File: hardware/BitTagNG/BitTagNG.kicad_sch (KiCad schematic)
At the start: 22 parts, among them J201 CONN_02X04, J301 Conn_01x01, J302 Conn_01x01, J303 Conn_01x01, J304 Conn_01x01, J401 CONN_01X02, Q501 Q_NPN_BEC, U1 at25ex321D-UUN, U2 adxl367, U302 stm32l431kc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

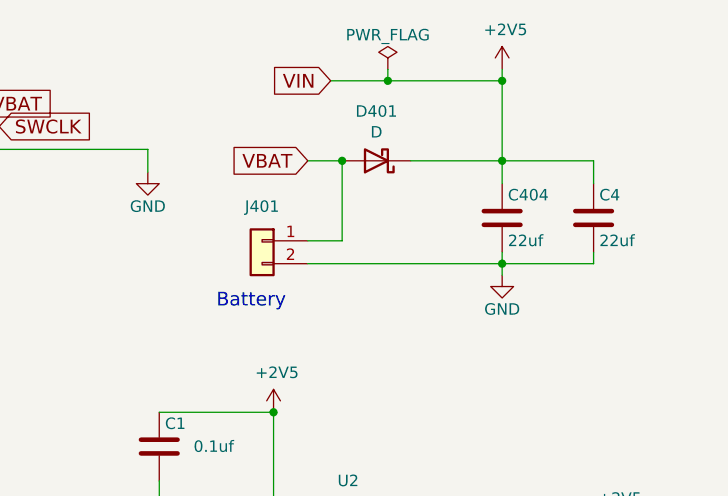
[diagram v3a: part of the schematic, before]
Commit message: added capacitor to BitTagNG
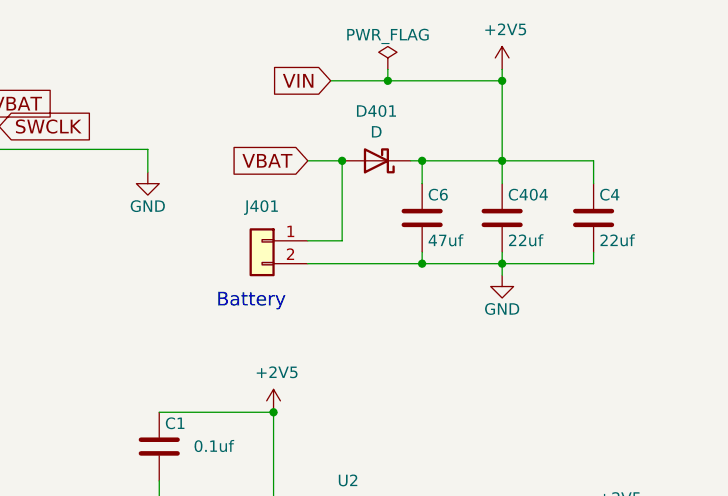
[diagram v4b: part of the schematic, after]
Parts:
- added C6: 47uf, Capacitor_SMD:C_0603_1608Metric, symbol Device:C
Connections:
- net +2V5: now also C6.1
- net GND: now also C6.2
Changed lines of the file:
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@@
   (junction (at 245.11 44.45) (diameter 0) (color 0 0 0 0)
+  )
+  (junction (at 236.22 44.45) (diameter 0) (color 0 0 0 0)
+  )
+  (junction (at 236.22 33.02) (diameter 0) (color 0 0 0 0)
   )
   (junction (at 74.93 30.48) (diameter 0) (color 0 0 0 0)
@@
     (stroke (width 0) (type default) (color 0 0 0 0))
   )
+  (wire (pts (xy 236.22 33.02) (xy 245.11 33.02))
+    (stroke (width 0) (type default) (color 0 0 0 0))
+  )
   (wire (pts (xy 104.14 49.53) (xy 110.49 49.53))
     (stroke (width 0) (type default) (color 0 0 0 0))
@@
     (stroke (width 0) (type default) (color 0 0 0 0))
   )
-  (wire (pts (xy 234.95 33.02) (xy 245.11 33.02))
+  (wire (pts (xy 234.95 33.02) (xy 236.22 33.02))
     (stroke (width 0) (type default) (color 0 0 0 0))
   )
@@
     (stroke (width 0) (type default) (color 0 0 0 0))
   )
+  (wire (pts (xy 236.22 35.56) (xy 236.22 33.02))
+    (stroke (width 0) (type default) (color 0 0 0 0))
+  )
   (wire (pts (xy 256.54 125.73) (xy 256.54 130.81))
     (stroke (width 0) (type default) (color 0 0 0 0))
@@
     (stroke (width 0) (type default) (color 0 0 0 0))
   )
+  (wire (pts (xy 236.22 44.45) (xy 245.11 44.45))
+    (stroke (width 0) (type default) (color 0 0 0 0))
+  )
   (wire (pts (xy 72.39 34.29) (xy 74.93 34.29))
     (stroke (width 0) (type default) (color 0 0 0 0))
   )
+  (wire (pts (xy 236.22 43.18) (xy 236.22 44.45))
+    (stroke (width 0) (type default) (color 0 0 0 0))
+  )
   (wire (pts (xy 245.11 91.44) (xy 245.11 93.98))
     (stroke (width 0) (type default) (color 0 0 0 0))
@@
     (stroke (width 0) (type default) (color 0 0 0 0))
   )
-  (wire (pts (xy 223.52 44.45) (xy 245.11 44.45))
+  (wire (pts (xy 223.52 44.45) (xy 236.22 44.45))
     (stroke (width 0) (type default) (color 0 0 0 0))
   )
@@
     (pin "1")
   )
+  (symbol (lib_id "Device:C") (at 236.22 39.37 0) (unit 1)
+    (in_bom yes) (on_board yes)
+    (property "Reference" "C6" (id 0) (at 236.855 36.83 0)
+      (effects (font (size 1.27 1.27)) (justify left))
+    )
+    (property "Value" "47uf" (id 1) (at 236.855 41.91 0)
+      (effects (font (size 1.27 1.27)) (justify left))
+    )
+    (property "Footprint" "Capacitor_SMD:C_0603_1608Metric" (id 2) (at 237.1852 43.18 0)
+      (effects (font (size 1.27 1.27)) hide)
+    )
+    (property "Datasheet" "~" (id 3) (at 236.22 39.37 0)
+      (effects (font (size 1.27 1.27)) hide)
+    )
+    (property "DISTPN" "478-11180-1-ND" (id 4) (at 236.22 39.37 0)
+      (effects (font (size 1.524 1.524)) hide)
+    )
+    (property "MFN" "KYOCERA AVX" (id 5) (at 236.22 39.37 0)
+      (effects (font (size 1.524 1.524)) hide)
+    )
+    (property "MPN" "06036D476MAT2A" (id 6) (at 236.22 39.37 0)
+      (effects (font (size 1.524 1.524)) hide)
+    )
+    (pin "1")
+    (pin "2")
+  )
   (symbol (lib_id "power:GND") (at 243.84 140.97 0) (unit 1)
     (in_bom yes) (on_board yes)
@@
       (reference "C5") (unit 1) (value "0.1uf") (footprint "Capacitor_SMD:C_0201_0603Metric")
     )
+    (path "/940d7541-e2e1-4c90-ba2c-739cfbe2bab8"
+      (reference "C6") (unit 1) (value "47uf") (footprint "Capacitor_SMD:C_0603_1608Metric")
+    )
     (path "/00000000-0000-0000-0000-00005c0f418b"
